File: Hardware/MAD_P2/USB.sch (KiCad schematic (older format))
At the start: 18 parts

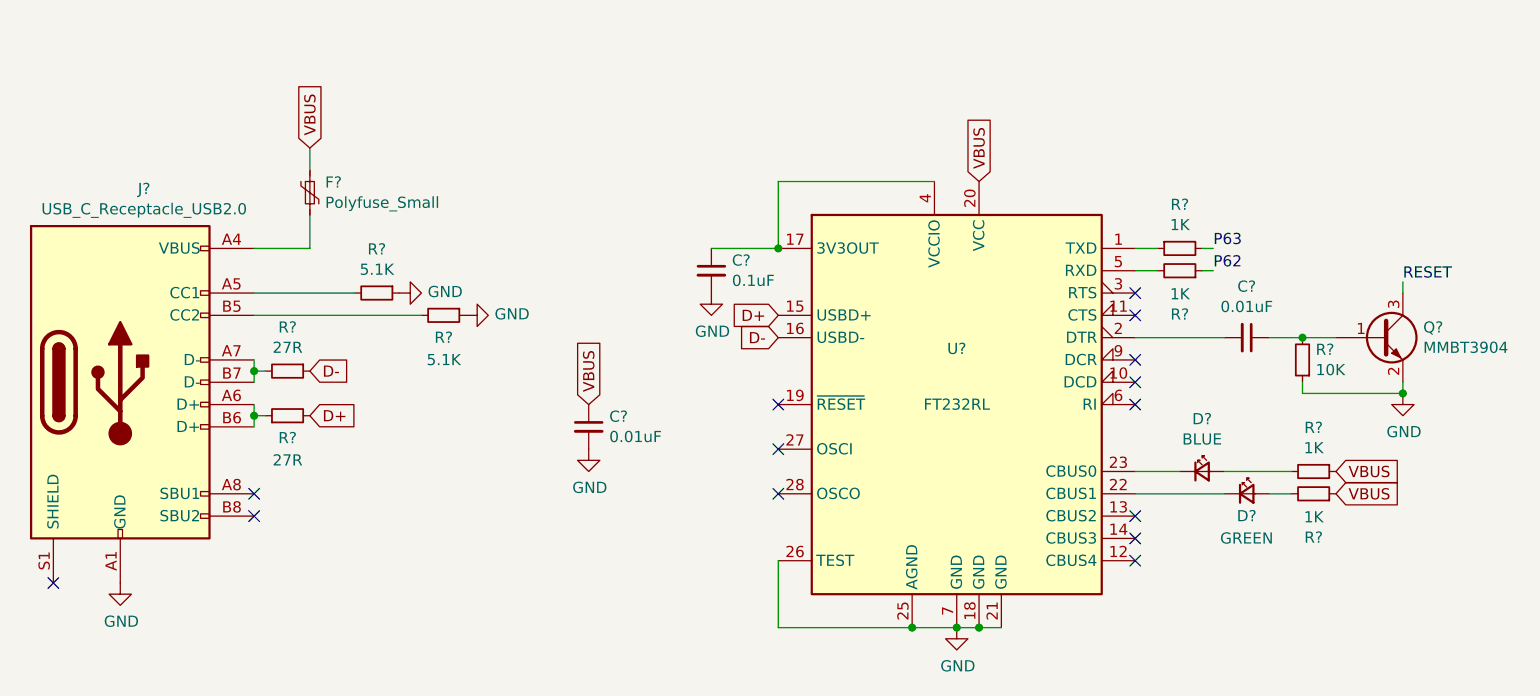
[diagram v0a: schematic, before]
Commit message: Added wifi to board
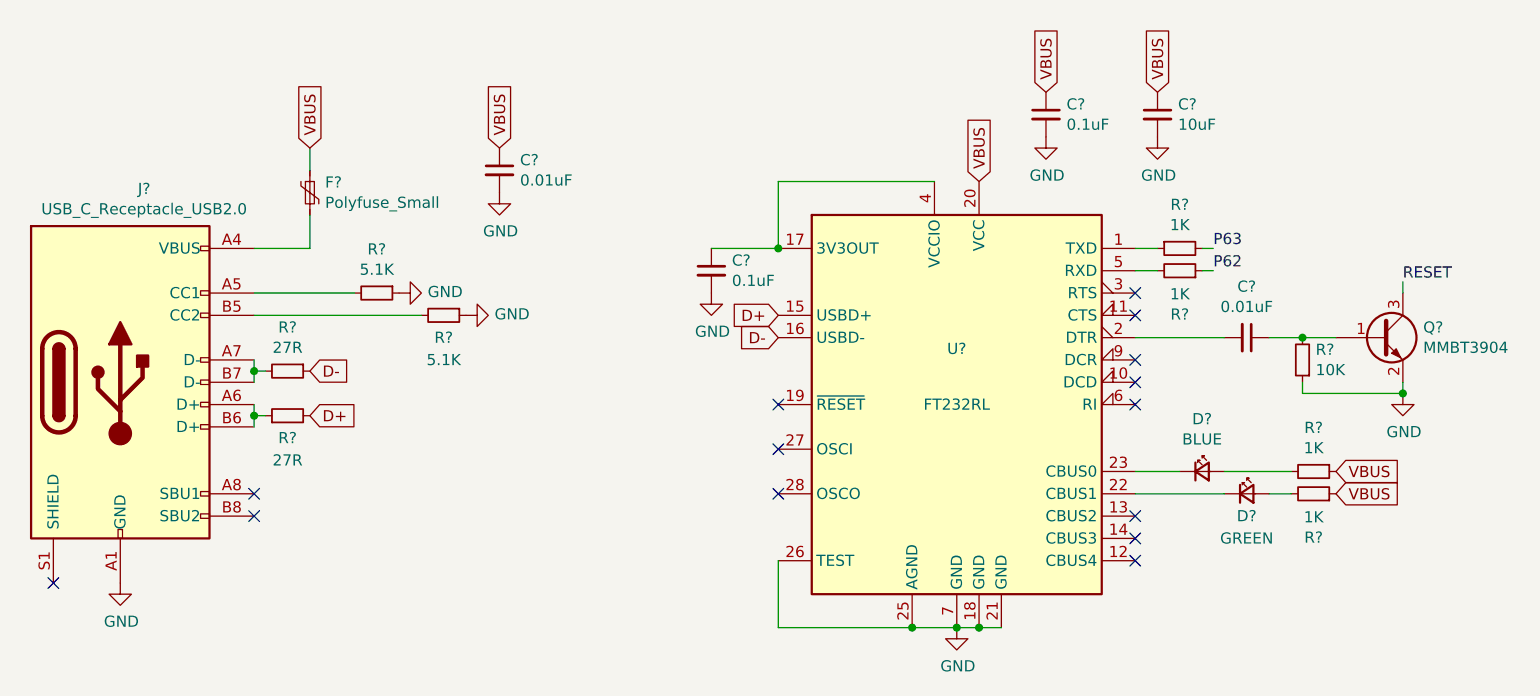
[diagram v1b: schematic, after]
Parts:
- added C?: 0.1uF, symbol Device:C_Small
- added C?: 10uF, symbol Device:C_Small
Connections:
- net GND: now also C?.2, C?.2
- net VBUS: now also C?.1, C?.1
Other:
- moved on the sheet: C?
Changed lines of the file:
@@
 $Descr A4 11693 8268
 encoding utf-8
-Sheet 5 5
+Sheet 5 7
 Title ""
 Date ""
@@
 L Device:C_Small C?
 U 1 1 60B8A93C
-P 5050 3750
-F 0 "C?" H 5142 3796 50  0000 L CNN
-F 1 "0.01uF" H 5142 3705 50  0000 L CNN
-F 2 "" H 5050 3750 50  0001 C CNN
-F 3 "~" H 5050 3750 50  0001 C CNN
-	1    5050 3750
+P 4650 2600
+F 0 "C?" H 4742 2646 50  0000 L CNN
+F 1 "0.01uF" H 4742 2555 50  0000 L CNN
+F 2 "" H 4650 2600 50  0001 C CNN
+F 3 "~" H 4650 2600 50  0001 C CNN
+	1    4650 2600
 	1    0    0    -1
 $EndComp
@@
 L power:GND #PWR?
 U 1 1 60B8C57B
-P 5050 3850
-F 0 "#PWR?" H 5050 3600 50  0001 C CNN
-F 1 "GND" H 5055 3677 50  0000 C CNN
-F 2 "" H 5050 3850 50  0001 C CNN
-F 3 "" H 5050 3850 50  0001 C CNN
-	1    5050 3850
-	1    0    0    -1
-$EndComp
-Text GLabel 5050 3650 1    50   Input ~ 0
+P 4650 2700
+F 0 "#PWR?" H 4650 2450 50  0001 C CNN
+F 1 "GND" H 4655 2527 50  0000 C CNN
+F 2 "" H 4650 2700 50  0001 C CNN
+F 3 "" H 4650 2700 50  0001 C CNN
+	1    4650 2700
+	1    0    0    -1
+$EndComp
+Text GLabel 4650 2500 1    50   Input ~ 0
 VBUS
 NoConn ~ 7500 3150
@@
 Wire Wire Line
 	7800 3050 7850 3050
+$Comp
+L Device:C_Small C?
+U 1 1 60BD791E
+P 7100 2350
+F 0 "C?" H 7192 2396 50  0000 L CNN
+F 1 "0.1uF" H 7192 2305 50  0000 L CNN
+F 2 "" H 7100 2350 50  0001 C CNN
+F 3 "~" H 7100 2350 50  0001 C CNN
+	1    7100 2350
+	1    0    0    -1
+$EndComp
+$Comp
+L power:GND #PWR?
+U 1 1 60BD7924
+P 7100 2450
+F 0 "#PWR?" H 7100 2200 50  0001 C CNN
+F 1 "GND" H 7105 2277 50  0000 C CNN
+F 2 "" H 7100 2450 50  0001 C CNN
+F 3 "" H 7100 2450 50  0001 C CNN
+	1    7100 2450
+	1    0    0    -1
+$EndComp
+Text GLabel 7100 2250 1    50   Input ~ 0
+VBUS
+$Comp
+L Device:C_Small C?
+U 1 1 60BD8956
+P 7600 2350
+F 0 "C?" H 7692 2396 50  0000 L CNN
+F 1 "10uF" H 7692 2305 50  0000 L CNN
+F 2 "" H 7600 2350 50  0001 C CNN
+F 3 "~" H 7600 2350 50  0001 C CNN
+	1    7600 2350
+	1    0    0    -1
+$EndComp
+$Comp
+L power:GND #PWR?
+U 1 1 60BD895C
+P 7600 2450
+F 0 "#PWR?" H 7600 2200 50  0001 C CNN
+F 1 "GND" H 7605 2277 50  0000 C CNN
+F 2 "" H 7600 2450 50  0001 C CNN
+F 3 "" H 7600 2450 50  0001 C CNN
+	1    7600 2450
+	1    0    0    -1
+$EndComp
+Text GLabel 7600 2250 1    50   Input ~ 0
+VBUS
 $EndSCHEMATC

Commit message: added adc
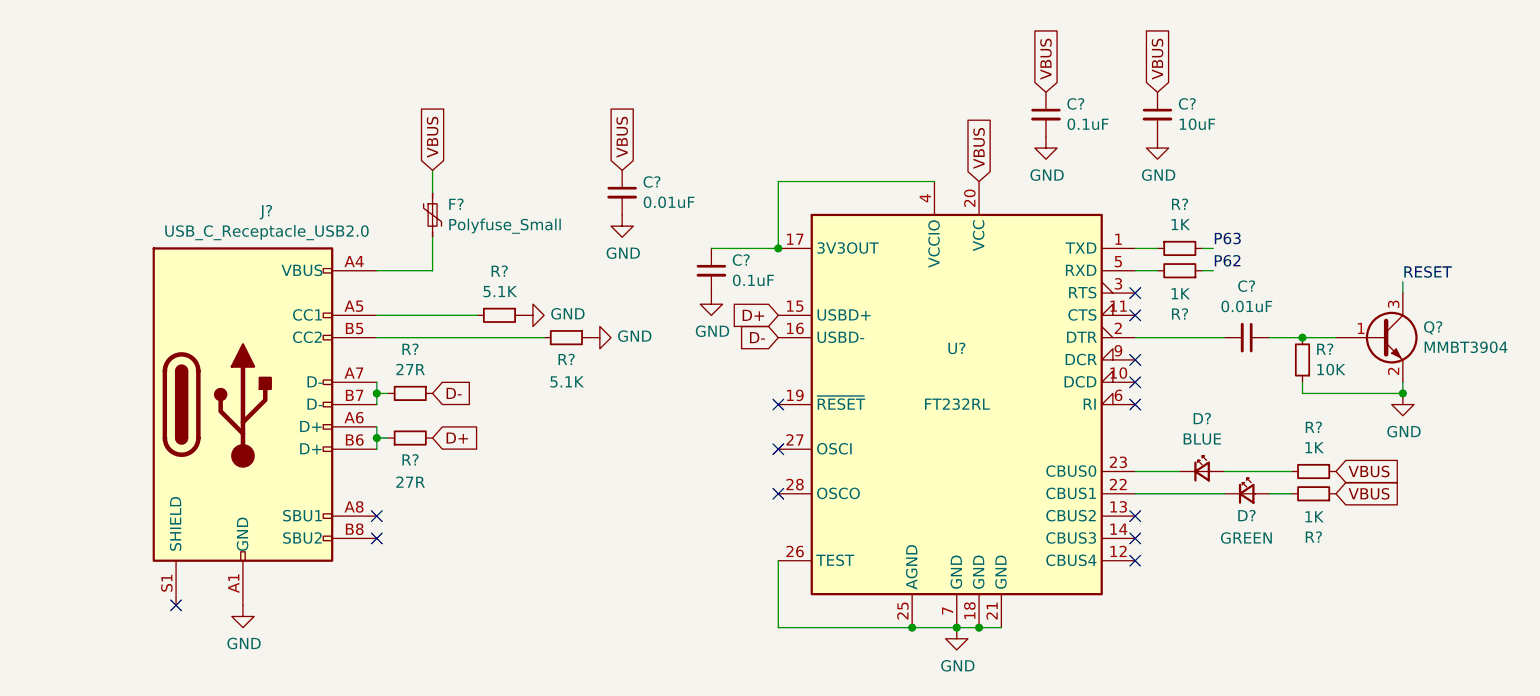
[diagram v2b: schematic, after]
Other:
- moved on the sheet: C?, F?, J?, R?
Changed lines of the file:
@@
 L Connector:USB_C_Receptacle_USB2.0 J?
 U 1 1 60B77A07
-P 2950 3550
-F 0 "J?" H 3057 4417 50  0000 C CNN
-F 1 "USB_C_Receptacle_USB2.0" H 3057 4326 50  0000 C CNN
-F 2 "" H 3100 3550 50  0001 C CNN
-F 3 "https://www.usb.org/sites/default/files/documents/usb_type-c.zip" H 3100 3550 50  0001 C CNN
-	1    2950 3550
+P 3500 3650
+F 0 "J?" H 3607 4517 50  0000 C CNN
+F 1 "USB_C_Receptacle_USB2.0" H 3607 4426 50  0000 C CNN
+F 2 "" H 3650 3650 50  0001 C CNN
+F 3 "https://www.usb.org/sites/default/files/documents/usb_type-c.zip" H 3650 3650 50  0001 C CNN
+	1    3500 3650
 	1    0    0    -1
 $EndComp
@@
 L Device:Polyfuse_Small F?
 U 1 1 60B796B1
-P 3800 2700
-F 0 "F?" H 3868 2746 50  0000 L CNN
-F 1 "Polyfuse_Small" H 3868 2655 50  0000 L CNN
-F 2 "" H 3850 2500 50  0001 L CNN
-F 3 "~" H 3800 2700 50  0001 C CNN
-	1    3800 2700
-	1    0    0    -1
-$EndComp
-Wire Wire Line
-	3550 2950 3800 2950
-Wire Wire Line
-	3800 2950 3800 2800
+P 4350 2800
+F 0 "F?" H 4418 2846 50  0000 L CNN
+F 1 "Polyfuse_Small" H 4418 2755 50  0000 L CNN
+F 2 "" H 4400 2600 50  0001 L CNN
+F 3 "~" H 4350 2800 50  0001 C CNN
+	1    4350 2800
+	1    0    0    -1
+$EndComp
+Wire Wire Line
+	4100 3050 4350 3050
+Wire Wire Line
+	4350 3050 4350 2900
 $Comp
 L Device:R_Small R?
 U 1 1 60B7AA43
-P 4100 3150
-F 0 "R?" V 3904 3150 50  0000 C CNN
-F 1 "5.1K" V 3995 3150 50  0000 C CNN
-F 2 "" H 4100 3150 50  0001 C CNN
-F 3 "~" H 4100 3150 50  0001 C CNN
-	1    4100 3150
+P 4650 3250
+F 0 "R?" V 4454 3250 50  0000 C CNN
+F 1 "5.1K" V 4545 3250 50  0000 C CNN
+F 2 "" H 4650 3250 50  0001 C CNN
+F 3 "~" H 4650 3250 50  0001 C CNN
+	1    4650 3250
 	0    1    1    0
 $EndComp
@@
 L Device:R_Small R?
 U 1 1 60B7B7AC
-P 4400 3250
-F 0 "R?" V 4500 3250 50  0000 C CNN
-F 1 "5.1K" V 4600 3250 50  0000 C CNN
-F 2 "" H 4400 3250 50  0001 C CNN
-F 3 "~" H 4400 3250 50  0001 C CNN
-	1    4400 3250
-	0    1    1    0
-$EndComp
-Wire Wire Line
-	3550 3250 4300 3250
-Wire Wire Line
-	3550 3150 4000 3150
+P 4950 3350
+F 0 "R?" V 5050 3350 50  0000 C CNN
+F 1 "5.1K" V 5150 3350 50  0000 C CNN
+F 2 "" H 4950 3350 50  0001 C CNN
+F 3 "~" H 4950 3350 50  0001 C CNN
+	1    4950 3350
+	0    1    1    0
+$EndComp
+Wire Wire Line
+	4100 3350 4850 3350
+Wire Wire Line
+	4100 3250 4550 3250
 $Comp
 L power:GND #PWR?
 U 1 1 60B7C574
-P 4500 3250
-F 0 "#PWR?" H 4500 3000 50  0001 C CNN
-F 1 "GND" V 4505 3122 50  0000 R CNN
-F 2 "" H 4500 3250 50  0001 C CNN
-F 3 "" H 4500 3250 50  0001 C CNN
-	1    4500 3250
+P 5050 3350
+F 0 "#PWR?" H 5050 3100 50  0001 C CNN
+F 1 "GND" V 5055 3222 50  0000 R CNN
+F 2 "" H 5050 3350 50  0001 C CNN
+F 3 "" H 5050 3350 50  0001 C CNN
+	1    5050 3350
 	0    -1   -1   0
 $EndComp
@@
 L power:GND #PWR?
 U 1 1 60B7CF7D
-P 4200 3150
-F 0 "#PWR?" H 4200 2900 50  0001 C CNN
-F 1 "GND" V 4205 3022 50  0000 R CNN
-F 2 "" H 4200 3150 50  0001 C CNN
-F 3 "" H 4200 3150 50  0001 C CNN
-	1    4200 3150
+P 4750 3250
+F 0 "#PWR?" H 4750 3000 50  0001 C CNN
+F 1 "GND" V 4755 3122 50  0000 R CNN
+F 2 "" H 4750 3250 50  0001 C CNN
+F 3 "" H 4750 3250 50  0001 C CNN
+	1    4750 3250
 	0    -1   -1   0
 $EndComp
 Wire Wire Line
-	3550 3550 3550 3500
-Wire Wire Line
-	3550 3750 3550 3700
+	4100 3650 4100 3600
+Wire Wire Line
+	4100 3850 4100 3800
 $Comp
 L power:GND #PWR?
 U 1 1 60B7D6CC
-P 2950 4450
-F 0 "#PWR?" H 2950 4200 50  0001 C CNN
-F 1 "GND" H 2955 4277 50  0000 C CNN
-F 2 "" H 2950 4450 50  0001 C CNN
-F 3 "" H 2950 4450 50  0001 C CNN
-	1    2950 4450
-	1    0    0    -1
-$EndComp
-NoConn ~ 2650 4450
-NoConn ~ 3550 4150
-NoConn ~ 3550 4050
-Text GLabel 3800 3700 2    50   Input ~ 0
+P 3500 4550
+F 0 "#PWR?" H 3500 4300 50  0001 C CNN
+F 1 "GND" H 3505 4377 50  0000 C CNN
+F 2 "" H 3500 4550 50  0001 C CNN
+F 3 "" H 3500 4550 50  0001 C CNN
+	1    3500 4550
+	1    0    0    -1
+$EndComp
+NoConn ~ 3200 4550
+NoConn ~ 4100 4250
+NoConn ~ 4100 4150
+Text GLabel 4350 3800 2    50   Input ~ 0
 D+
 Wire Wire Line
-	3550 3500 3600 3500
-Connection ~ 3550 3500
-Wire Wire Line
-	3550 3500 3550 3450
-Wire Wire Line
-	3550 3700 3600 3700
-Connection ~ 3550 3700
-Wire Wire Line
-	3550 3700 3550 3650
-Text GLabel 3800 3500 2    50   Input ~ 0
+	4100 3600 4150 3600
+Connection ~ 4100 3600
+Wire Wire Line
+	4100 3600 4100 3550
+Wire Wire Line
+	4100 3800 4150 3800
+Connection ~ 4100 3800
+Wire Wire Line
+	4100 3800 4100 3750
+Text GLabel 4350 3600 2    50   Input ~ 0
 D-
-Text GLabel 3800 2500 1    50   Input ~ 0
-VBUS
-Wire Wire Line
-	3800 2500 3800 2600
+Text GLabel 4350 2600 1    50   Input ~ 0
+VBUS
+Wire Wire Line
+	4350 2600 4350 2700
 $Comp
 L Interface_USB:FT232RL U?
@@
 L Device:C_Small C?
 U 1 1 60B8A93C
-P 4650 2600
-F 0 "C?" H 4742 2646 50  0000 L CNN
-F 1 "0.01uF" H 4742 2555 50  0000 L CNN
-F 2 "" H 4650 2600 50  0001 C CNN
-F 3 "~" H 4650 2600 50  0001 C CNN
-	1    4650 2600
+P 5200 2700
+F 0 "C?" H 5292 2746 50  0000 L CNN
+F 1 "0.01uF" H 5292 2655 50  0000 L CNN
+F 2 "" H 5200 2700 50  0001 C CNN
+F 3 "~" H 5200 2700 50  0001 C CNN
+	1    5200 2700
 	1    0    0    -1
 $EndComp
@@
 L power:GND #PWR?
 U 1 1 60B8C57B
-P 4650 2700
-F 0 "#PWR?" H 4650 2450 50  0001 C CNN
-F 1 "GND" H 4655 2527 50  0000 C CNN
-F 2 "" H 4650 2700 50  0001 C CNN
-F 3 "" H 4650 2700 50  0001 C CNN
-	1    4650 2700
-	1    0    0    -1
-$EndComp
-Text GLabel 4650 2500 1    50   Input ~ 0
+P 5200 2800
+F 0 "#PWR?" H 5200 2550 50  0001 C CNN
+F 1 "GND" H 5205 2627 50  0000 C CNN
+F 2 "" H 5200 2800 50  0001 C CNN
+F 3 "" H 5200 2800 50  0001 C CNN
+	1    5200 2800
+	1    0    0    -1
+$EndComp
+Text GLabel 5200 2600 1    50   Input ~ 0
 VBUS
 NoConn ~ 7500 3150
@@
 L Device:R_Small R?
 U 1 1 60BC2280
-P 3700 3500
-F 0 "R?" V 3504 3500 50  0000 C CNN
-F 1 "27R" V 3595 3500 50  0000 C CNN
-F 2 "" H 3700 3500 50  0001 C CNN
-F 3 "~" H 3700 3500 50  0001 C CNN
-	1    3700 3500
+P 4250 3600
+F 0 "R?" V 4054 3600 50  0000 C CNN
+F 1 "27R" V 4145 3600 50  0000 C CNN
+F 2 "" H 4250 3600 50  0001 C CNN
+F 3 "~" H 4250 3600 50  0001 C CNN
+	1    4250 3600
 	0    1    1    0
 $EndComp
@@
 L Device:R_Small R?
 U 1 1 60BC2815
-P 3700 3700
-F 0 "R?" V 3600 3700 50  0000 C CNN
-F 1 "27R" V 3500 3700 50  0000 C CNN
-F 2 "" H 3700 3700 50  0001 C CNN
-F 3 "~" H 3700 3700 50  0001 C CNN
-	1    3700 3700
+P 4250 3800
+F 0 "R?" V 4150 3800 50  0000 C CNN
+F 1 "27R" V 4050 3800 50  0000 C CNN
+F 2 "" H 4250 3800 50  0001 C CNN
+F 3 "~" H 4250 3800 50  0001 C CNN
+	1    4250 3800
 	0    -1   -1   0
 $EndComp
